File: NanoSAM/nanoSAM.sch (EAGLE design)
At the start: 111 parts, among them J1 POWER_JACK, U1 LTC3260EMSEPBF, U2 LMV324

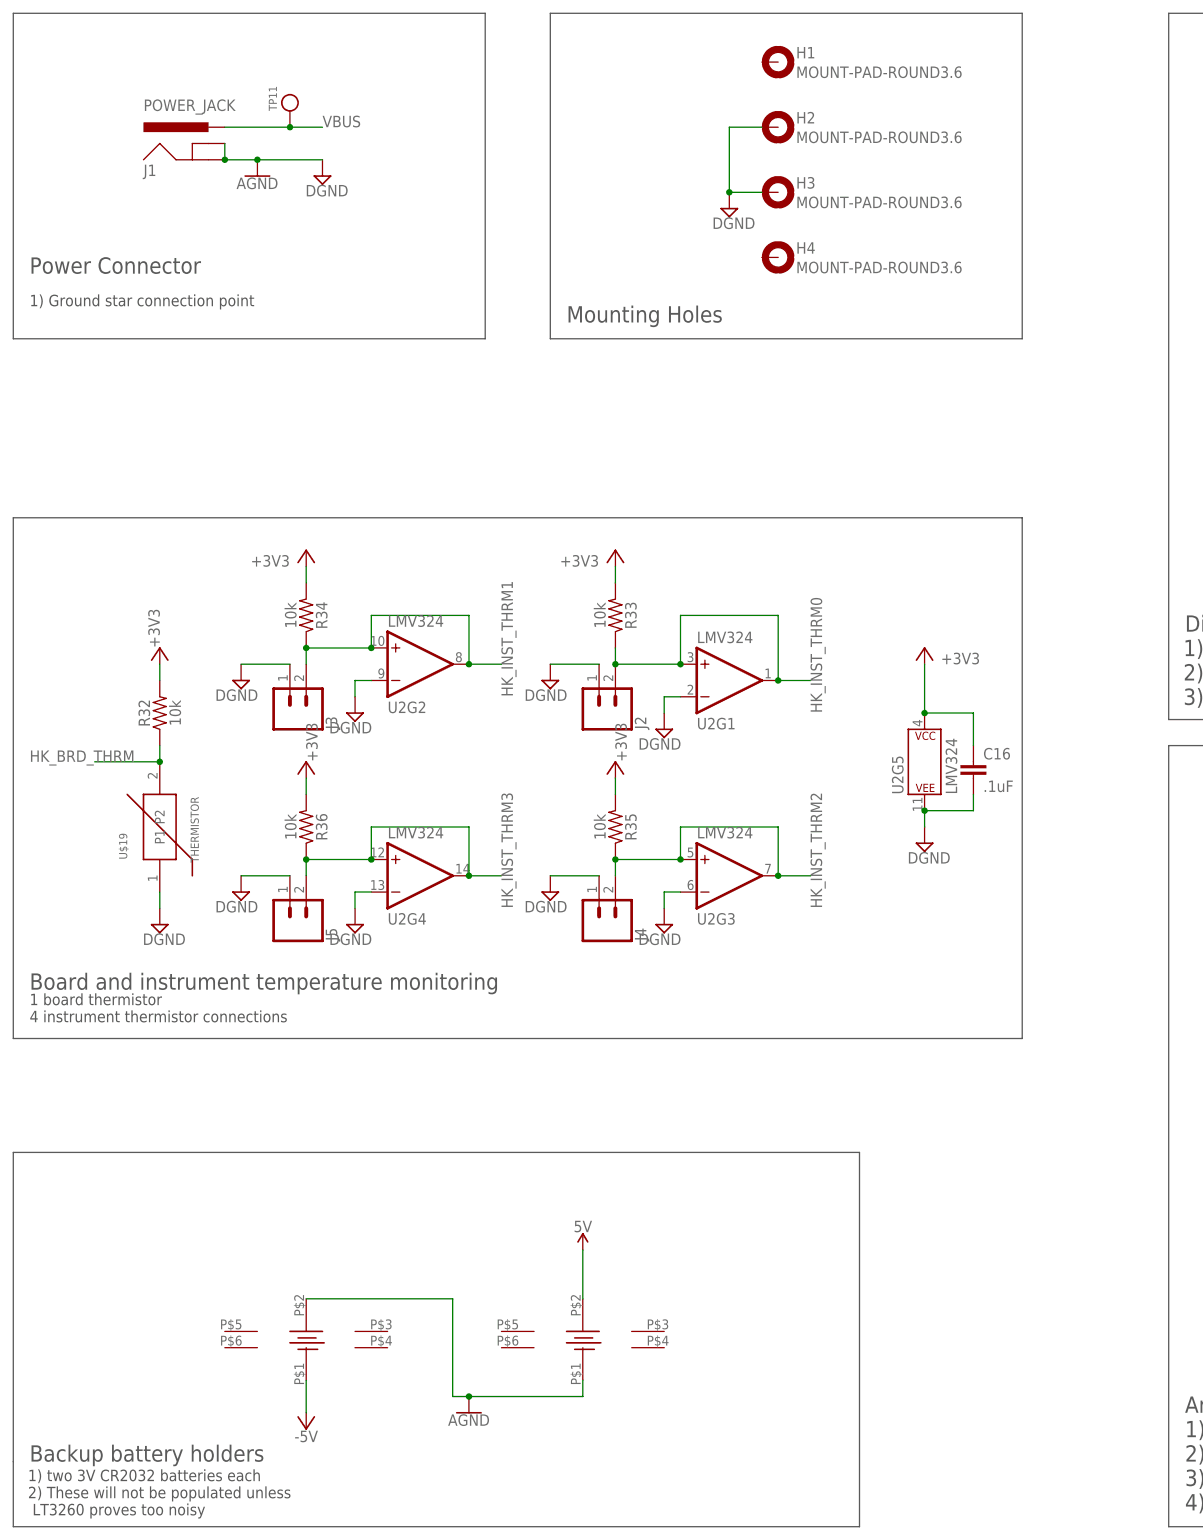
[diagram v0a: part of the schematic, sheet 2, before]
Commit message: Added HK Capacitors
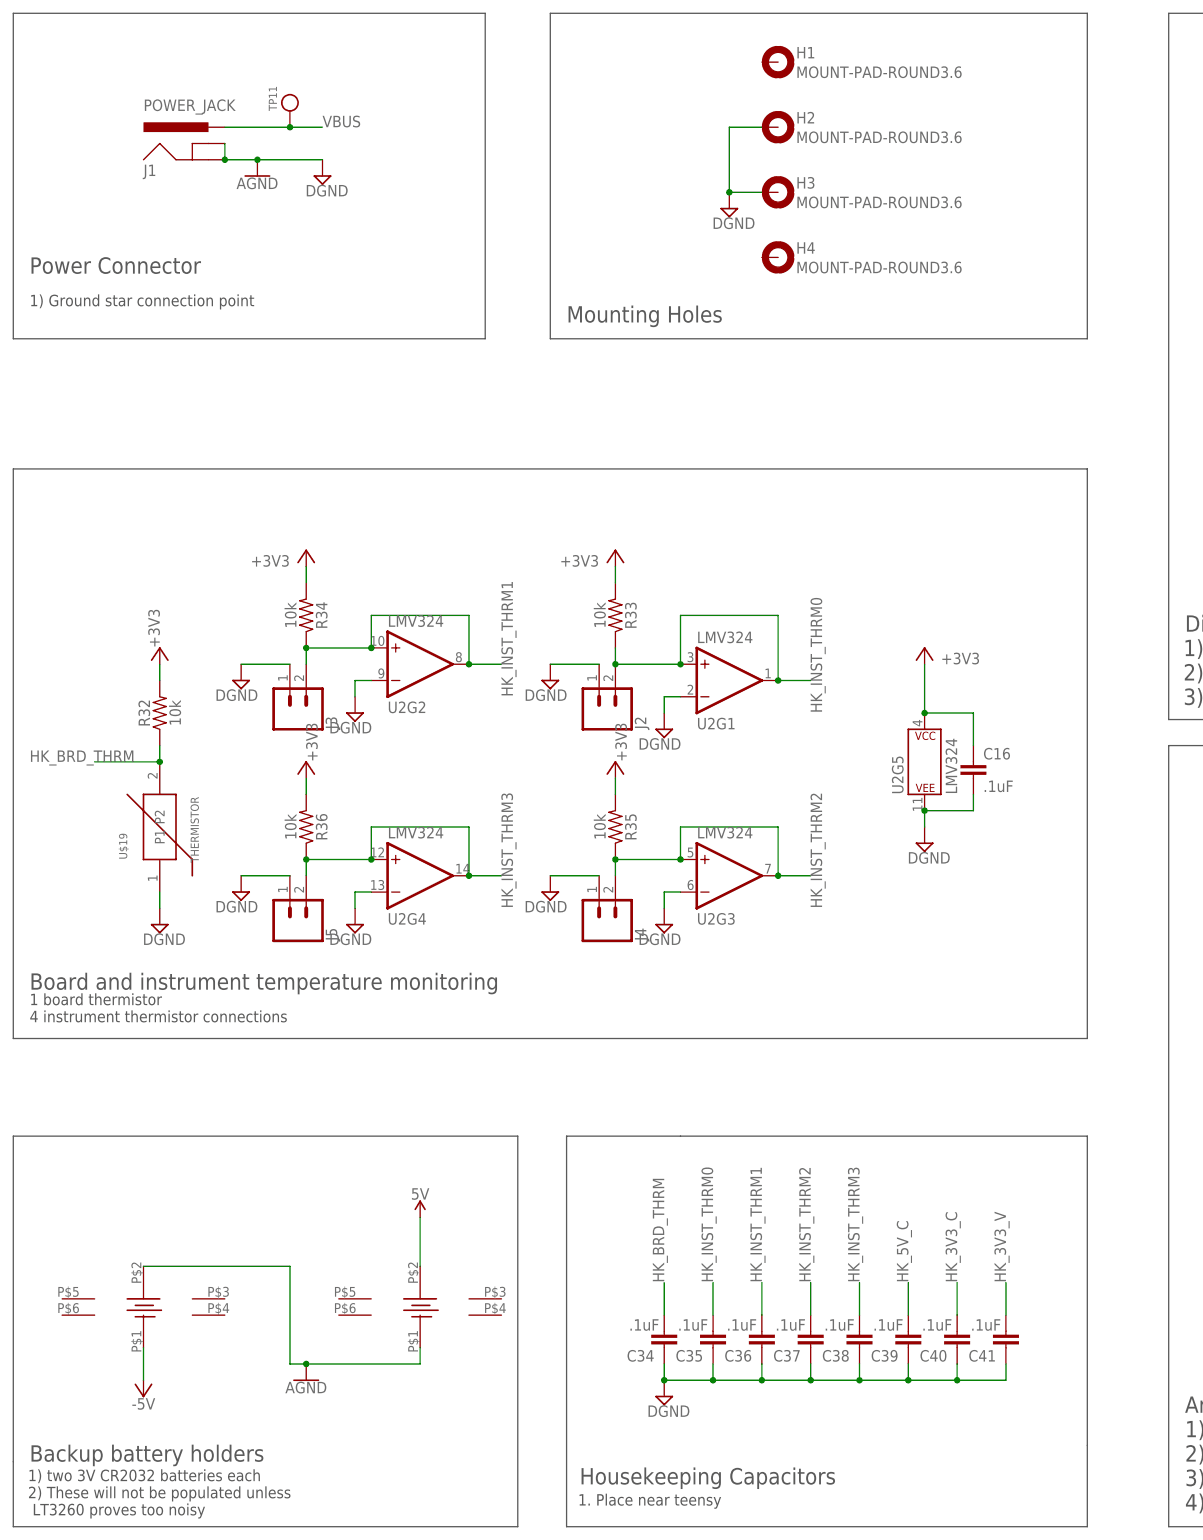
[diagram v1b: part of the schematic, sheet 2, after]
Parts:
- added C34, C35, C36, C37, C38, C39, C40, C41: .1uF, SparkFun-Capacitors:0.1UF-0603-25V-5%
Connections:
- net DGND: now also C34.1, C35.1, C36.1, C37.1, C38.1, C39.1, C40.1, C41.1
- net HK_3V3_C: now also C40.2
- net HK_3V3_V: now also C41.2
- net HK_5V_C: now also C39.2
- net HK_BRD_THRM: now also C34.2
- net HK_INST_THRM0: now also C35.2
- net HK_INST_THRM1: now also C36.2
- net HK_INST_THRM2: now also C37.2
- net HK_INST_THRM3: now also C38.2
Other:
- note added: "1. Place near teensy"
- note added: "Housekeeping Capacitors"

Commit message: fixed some PCB issues
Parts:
- C16: value .1uF -> 1uF; device SparkFun-Capacitors:4.7UF-1206-16V-(+80/-20%) -> SparkFun-Capacitors:4.7UF0603
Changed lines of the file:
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@@
 <?xml version="1.0" encoding="utf-8"?>
 <!DOCTYPE eagle SYSTEM "eagle.dtd">
-<eagle version="9.5.1">
+<eagle version="9.3.0">
 <drawing>
 <settings>
@@
 <grid distance="0.1" unitdist="inch" unit="inch" style="lines" multiple="1" display="no" altdistance="0.01" altunitdist="inch" altunit="inch"/>
 <layers>
-<layer number="1" name="Top" color="4" fill="1" visible="no" active="no"/>
-<layer number="2" name="Route2" color="16" fill="1" visible="no" active="no"/>
-<layer number="3" name="Route3" color="17" fill="1" visible="no" active="no"/>
-<layer number="4" name="Route4" color="18" fill="1" visible="no" active="no"/>
-<layer number="5" name="Route5" color="19" fill="1" visible="no" active="no"/>
-<layer number="6" name="Route6" color="25" fill="1" visible="no" active="no"/>
-<layer number="7" name="Route7" color="26" fill="1" visible="no" active="no"/>
-<layer number="8" name="Route8" color="27" fill="1" visible="no" active="no"/>
-<layer number="9" name="Route9" color="28" fill="1" visible="no" active="no"/>
-<layer number="10" name="Route10" color="29" fill="1" visible="no" active="no"/>
-<layer number="11" name="Route11" color="30" fill="1" visible="no" active="no"/>
-<layer number="12" name="Route12" color="20" fill="1" visible="no" active="no"/>
-<layer number="13" name="Route13" color="21" fill="1" visible="no" active="no"/>
-<layer number="14" name="Route14" color="22" fill="1" visible="no" active="no"/>
-<layer number="15" name="Route15" color="23" fill="1" visible="no" active="no"/>
-<layer number="16" name="Bottom" color="1" fill="1" visible="no" active="no"/>
-<layer number="17" name="Pads" color="2" fill="1" visible="no" active="no"/>
-<layer number="18" name="Vias" color="2" fill="1" visible="no" active="no"/>
-<layer number="19" name="Unrouted" color="6" fill="1" visible="no" active="no"/>
-<layer number="20" name="Dimension" color="24" fill="1" visible="no" active="no"/>
-<layer number="21" name="tPlace" color="7" fill="1" visible="no" active="no"/>
-<layer number="22" name="bPlace" color="7" fill="1" visible="no" active="no"/>
-<layer number="23" name="tOrigins" color="15" fill="1" visible="no" active="no"/>
-<layer number="24" name="bOrigins" color="15" fill="1" visible="no" active="no"/>
-<layer number="25" name="tNames" color="7" fill="1" visible="no" active="no"/>
-<layer number="26" name="bNames" color="7" fill="1" visible="no" active="no"/>
-<layer number="27" name="tValues" color="7" fill="1" visible="no" active="no"/>
-<layer number="28" name="bValues" color="7" fill="1" visible="no" active="no"/>
+<layer number="1" name="Top" color="4" fill="1" visible="yes" active="no"/>
+<layer number="2" name="Route2" color="16" fill="1" visible="yes" active="no"/>
+<layer number="3" name="Route3" color="17" fill="1" visible="yes" active="no"/>
+<layer number="4" name="Route4" color="18" fill="1" visible="yes" active="no"/>
+<layer number="5" name="Route5" color="19" fill="1" visible="yes" active="no"/>
+<layer number="6" name="Route6" color="25" fill="1" visible="yes" active="no"/>
+<layer number="7" name="Route7" color="26" fill="1" visible="yes" active="no"/>
+<layer number="8" name="Route8" color="27" fill="1" visible="yes" active="no"/>
+<layer number="9" name="Route9" color="28" fill="1" visible="yes" active="no"/>
+<layer number="10" name="Route10" color="29" fill="1" visible="yes" active="no"/>
+<layer number="11" name="Route11" color="30" fill="1" visible="yes" active="no"/>
+<layer number="12" name="Route12" color="20" fill="1" visible="yes" active="no"/>
+<layer number="13" name="Route13" color="21" fill="1" visible="yes" active="no"/>
+<layer number="14" name="Route14" color="22" fill="1" visible="yes" active="no"/>
+<layer number="15" name="Route15" color="23" fill="1" visible="yes" active="no"/>
+<layer number="16" name="Bottom" color="1" fill="1" visible="yes" active="no"/>
+<layer number="17" name="Pads" color="2" fill="1" visible="yes" active="no"/>
+<layer number="18" name="Vias" color="2" fill="1" visible="yes" active="no"/>
+<layer number="19" name="Unrouted" color="6" fill="1" visible="yes" active="no"/>
+<layer number="20" name="Dimension" color="24" fill="1" visible="yes" active="no"/>
+<layer number="21" name="tPlace" color="7" fill="1" visible="yes" active="no"/>
+<layer number="22" name="bPlace" color="7" fill="1" visible="yes" active="no"/>
+<layer number="23" name="tOrigins" color="15" fill="1" visible="yes" active="no"/>
+<layer number="24" name="bOrigins" color="15" fill="1" visible="yes" active="no"/>
+<layer number="25" name="tNames" color="7" fill="1" visible="yes" active="no"/>
+<layer number="26" name="bNames" color="7" fill="1" visible="yes" active="no"/>
+<layer number="27" name="tValues" color="7" fill="1" visible="yes" active="no"/>
+<layer number="28" name="bValues" color="7" fill="1" visible="yes" active="no"/>
 <layer number="29" name="tStop" color="7" fill="3" visible="no" active="no"/>
 <layer number="30" name="bStop" color="7" fill="6" visible="no" active="no"/>
@@
 <layer number="35" name="tGlue" color="7" fill="4" visible="no" active="no"/>
 <layer number="36" name="bGlue" color="7" fill="5" visible="no" active="no"/>
-<layer number="37" name="tTest" color="7" fill="1" visible="no" active="no"/>
-<layer number="38" name="bTest" color="7" fill="1" visible="no" active="no"/>
+<layer number="37" name="tTest" color="7" fill="1" visible="yes" active="no"/>
+<layer number="38" name="bTest" color="7" fill="1" visible="yes" active="no"/>
 <layer number="39" name="tKeepout" color="4" fill="11" visible="no" active="no"/>
 <layer number="40" name="bKeepout" color="1" fill="11" visible="no" active="no"/>
@@
 <layer number="44" name="Drills" color="7" fill="1" visible="no" active="no"/>
 <layer number="45" name="Holes" color="7" fill="1" visible="no" active="no"/>
-<layer number="46" name="Milling" color="3" fill="1" visible="no" active="no"/>
-<layer number="47" name="Measures" color="7" fill="1" visible="no" active="no"/>
-<layer number="48" name="Document" color="7" fill="1" visible="no" active="no"/>
-<layer number="49" name="Reference" color="7" fill="1" visible="no" active="no"/>
-<layer number="50" name="dxf" color="7" fill="1" visible="no" active="no"/>
-<layer number="51" name="tDocu" color="7" fill="1" visible="no" active="no"/>
-<layer number="52" name="bDocu" color="7" fill="1" visible="no" active="no"/>
-<layer number="53" name="tGND_GNDA" color="7" fill="9" visible="no" active="no"/>
-<layer number="54" name="bGND_GNDA" color="1" fill="9" visible="no" active="no"/>
-<layer number="56" name="wert" color="7" fill="1" visible="no" active="no"/>
-<layer number="57" name="tCAD" color="7" fill="1" visible="no" active="no"/>
-<layer number="59" name="tCarbon" color="7" fill="1" visible="no" active="no"/>
-<layer number="60" name="bCarbon" color="7" fill="1" visible="no" active="no"/>
+<layer number="46" name="Milling" color="3" fill="1" visible="yes" active="no"/>
+<layer number="47" name="Measures" color="7" fill="1" visible="yes" active="no"/>
+<layer number="48" name="Document" color="7" fill="1" visible="yes" active="no"/>
+<layer number="49" name="Reference" color="7" fill="1" visible="yes" active="no"/>
+<layer number="50" name="dxf" color="7" fill="1" visible="yes" active="no"/>
+<layer number="51" name="tDocu" color="7" fill="1" visible="yes" active="no"/>
+<layer number="52" name="bDocu" color="7" fill="1" visible="yes" active="no"/>
+<layer number="53" name="tGND_GNDA" color="7" fill="9" visible="yes" active="no"/>
+<layer number="54" name="bGND_GNDA" color="1" fill="9" visible="yes" active="no"/>
+<layer number="56" name="wert" color="7" fill="1" visible="yes" active="no"/>
+<layer number="57" name="tCAD" color="7" fill="1" visible="yes" active="no"/>
+<layer number="59" name="tCarbon" color="7" fill="1" visible="yes" active="no"/>
+<layer number="60" name="bCarbon" color="7" fill="1" visible="yes" active="no"/>
 <layer number="88" name="SimResults" color="9" fill="1" visible="yes" active="yes"/>
 <layer number="89" name="SimProbes" color="9" fill="1" visible="yes" active="yes"/>
@@
 <part name="SUPPLY36" library="supply2" library_urn="urn:adsk.eagle:library:372" deviceset="DGND" device=""/>
 <part name="+3V5" library="supply1" library_urn="urn:adsk.eagle:library:371" deviceset="+3V3" device=""/>
-<part name="C16" library="SparkFun-Capacitors" library_urn="urn:adsk.eagle:library:510" deviceset="4.7UF" device="-1206-16V-(+80/-20%)" package3d_urn="urn:adsk.eagle:package:37426/1" value=".1uF"/>
+<part name="C16" library="SparkFun-Capacitors" library_urn="urn:adsk.eagle:library:510" deviceset="4.7UF" device="0603" package3d_urn="urn:adsk.eagle:package:37414/1" value="1uF"/>
 <part name="C17" library="SparkFun-Capacitors" library_urn="urn:adsk.eagle:library:510" deviceset="0.1UF" device="-0603-25V-5%" package3d_urn="urn:adsk.eagle:package:37414/1" value="0.1uF"/>
 <part name="C18" library="SparkFun-Capacitors" library_urn="urn:adsk.eagle:library:510" deviceset="0.1UF" device="-0603-25V-5%" package3d_urn="urn:adsk.eagle:package:37414/1" value="0.1uF"/>

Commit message: updated some values
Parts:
- C24, C4: value 4.7uF -> 4.7uF - 25V
- R14: value (none) -> 5k
- R15: value (none) -> 10k
- R29: value (none) -> 0
